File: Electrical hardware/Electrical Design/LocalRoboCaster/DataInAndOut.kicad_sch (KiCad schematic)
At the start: 51 parts, among them J2 Conn_01x02_Pin, J4 Conn_01x04_Pin, J5 Conn_01x04_Pin, M1 Fan, M3 PC Fan, M5 PC Fan, Q4 IRLZ44NPBF, Q5 IRL3705NPBF, Q6 IRLZ44NPBF, Q7 IRLZ44NPBF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

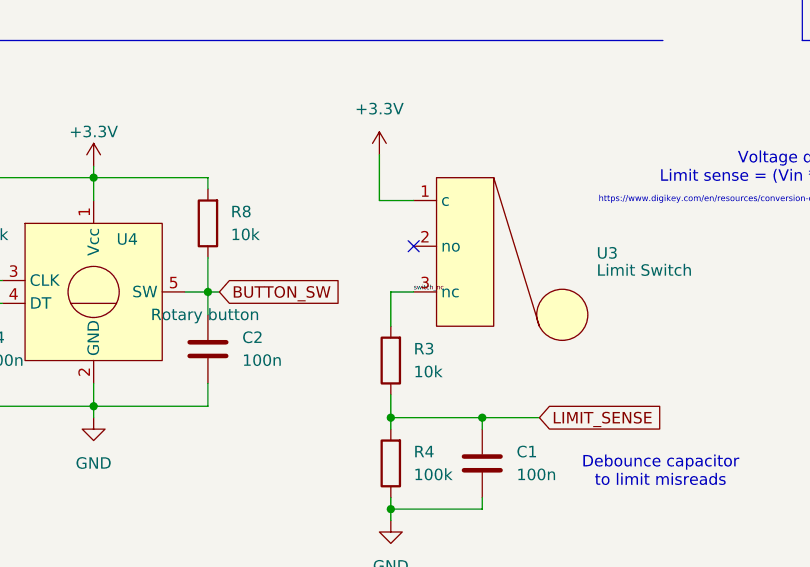
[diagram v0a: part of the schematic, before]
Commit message: Added report and improved electrical design files
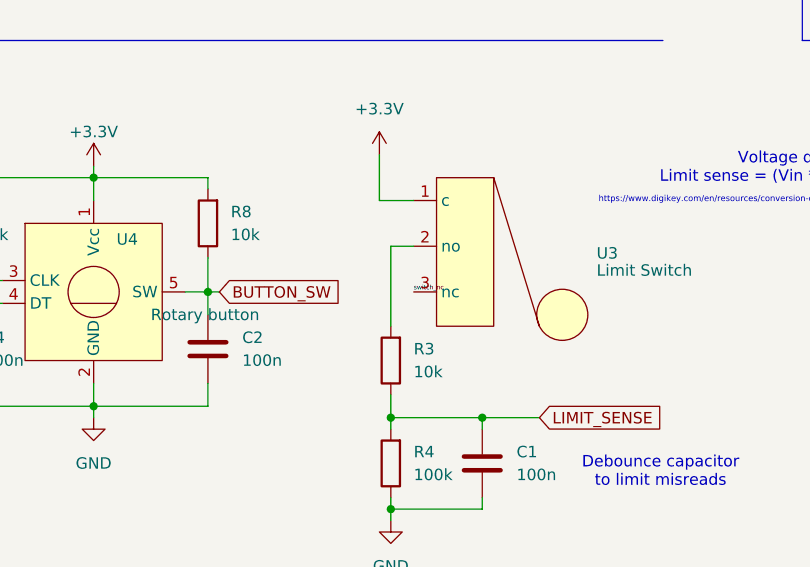
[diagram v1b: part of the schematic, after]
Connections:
- net switch_nc: no longer R3.2
- net at U3.2 (no): now also R3.2
- no-connect marks 1 -> 0
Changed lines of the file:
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@@
 		(color 0 0 0 0)
 	)
-	(no_connect
-		(at 127 153.67)
+	(wire
+		(pts
+			(xy 124.46 153.67) (xy 124.46 162.56)
+		)
+		(stroke
+			(width 0)
+			(type default)
+		)
 	)
 	(wire
@@
 	(wire
 		(pts
+			(xy 124.46 153.67) (xy 127 153.67)
+		)
+		(stroke
+			(width 0)
+			(type default)
+		)
+	)
+	(wire
+		(pts
 			(xy 185.42 66.04) (xy 194.31 66.04)
 		)
@@
 	(wire
 		(pts
-			(xy 124.46 158.75) (xy 127 158.75)
-		)
-		(stroke
-			(width 0)
-			(type default)
-		)
-	)
-	(wire
-		(pts
 			(xy 124.46 172.72) (xy 124.46 170.18)
 		)
@@
 		)
 		(stroke
-			(width 0)
-			(type default)
-		)
-	)
-	(wire
-		(pts
-			(xy 124.46 158.75) (xy 124.46 162.56)
-		)
-		(stroke
